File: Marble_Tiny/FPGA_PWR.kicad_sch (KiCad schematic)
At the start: 52 parts, among them U1 XC7A35T-CSG325

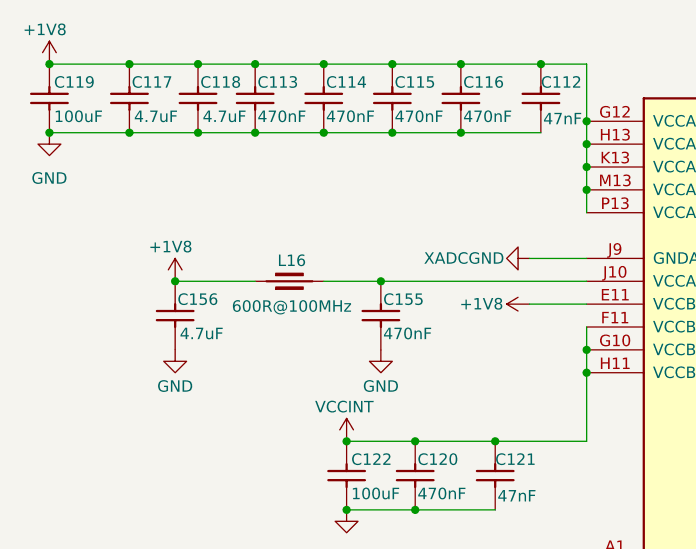
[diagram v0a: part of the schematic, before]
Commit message: components placement done, fixed issue with PCB
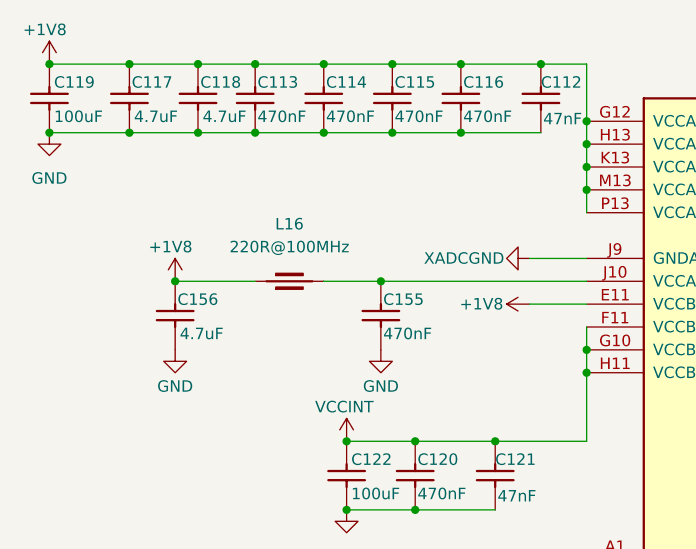
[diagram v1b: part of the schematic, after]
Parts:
- removed L16: IND0603_MURATA_BLM18AG601SN1, Inductors SMD:INDC1608X95N, symbol Inductors SMD:IND0603_MURATA_BLM18AG601SN1
- added L16: IND0402_MURATA_BLM15HB221SN1, Inductors SMD:INDC1005X55N, symbol Inductors SMD:IND0402_MURATA_BLM15HB221SN1
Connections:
- net +1V8: now also L16.1
- net at C155.2, U1.J10 (VCCADC_0): now also L16.2
